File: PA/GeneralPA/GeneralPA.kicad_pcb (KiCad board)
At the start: 2 copper layers, 170.2 x 80.3 mm, 117 parts, among them J2 RFin, J3 RFout, J4 FAN, J5 SWR, J6 48v_PAD, J7 48v_PAD, Q1 2N3904, Q2 IRF510, Q3 IRF510, Q4 IRF510, Q5 2sc5706, Q6 BC548, T1 Transformer_1P_1S, T2 Transformer_1P_1S, T3 Transformer_T100, U1 LM317HVT, U2 LM7809_TO220

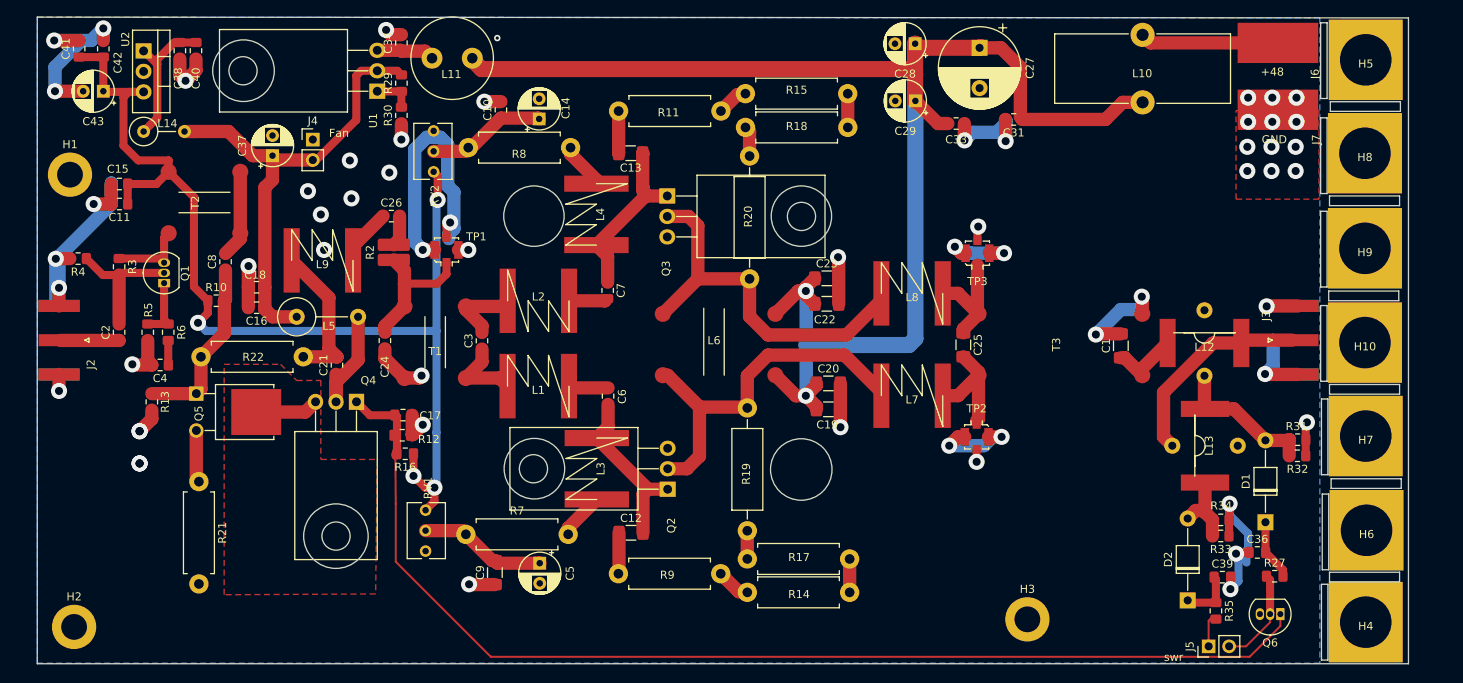
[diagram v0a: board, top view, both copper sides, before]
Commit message: update 2nd version of PA, adding some driver ciruits
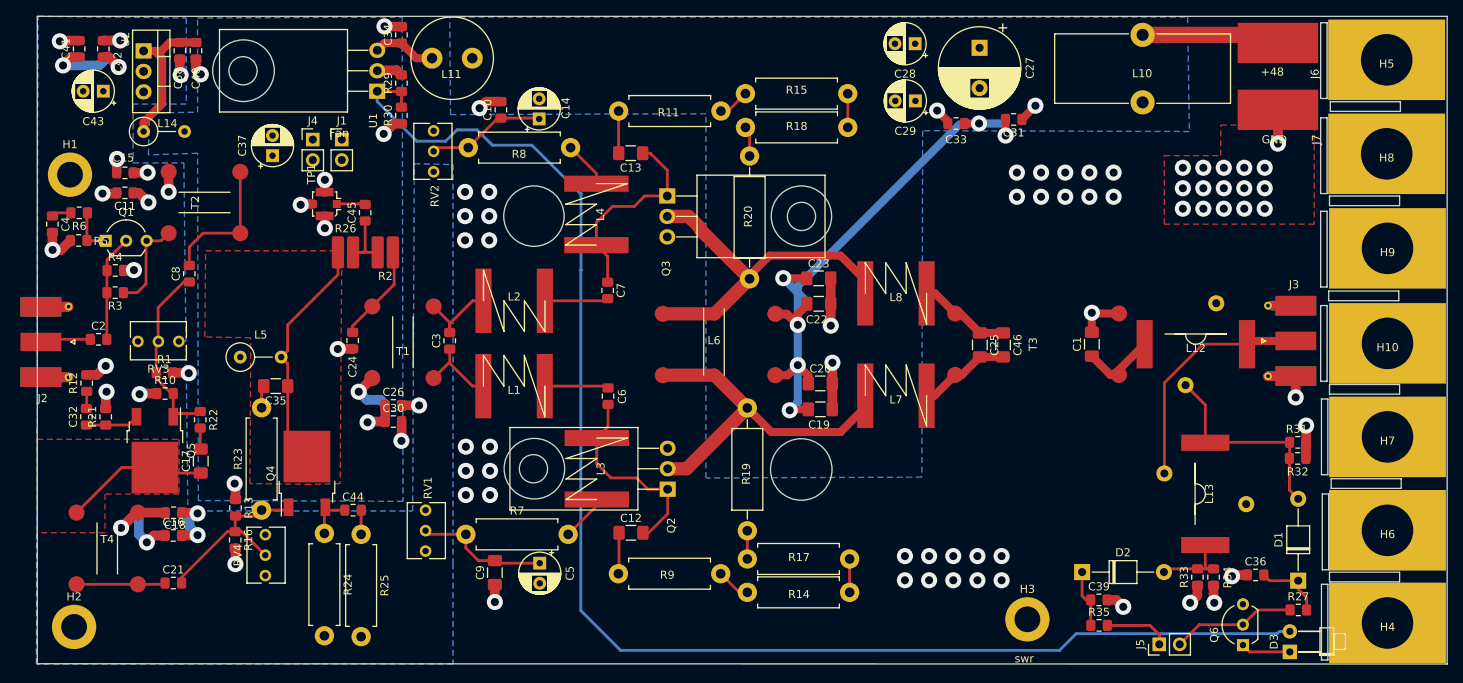
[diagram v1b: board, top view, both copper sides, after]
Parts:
- removed L9: 33n, Myfootprint:HomeMade_L_aircore
- removed TP2, TP3: Conn_Coaxial, Connector_Coaxial:U.FL_Molex_MCRF_73412-0110_Vertical
- added C30: 10n, Capacitor_SMD:C_0805_2012Metric_Pad1.15x1.40mm_HandSolder, F.Cu at (95.0, 101.0)
- added C32: 100n, Capacitor_SMD:C_0805_2012Metric_Pad1.15x1.40mm_HandSolder, F.Cu at (56.9, 100.4)
- added C35: 10u, Capacitor_SMD:C_1206_3216Metric_Pad1.42x1.75mm_HandSolder, F.Cu at (80.4, 96.6)
- added C44: 100n, Capacitor_SMD:C_0805_2012Metric_Pad1.15x1.40mm_HandSolder, F.Cu at (90.0, 112.0)
- added C45: 0.1u, Capacitor_SMD:C_0805_2012Metric_Pad1.15x1.40mm_HandSolder, F.Cu at (91.5, 75.1)
- added C46: 150p, Capacitor_SMD:C_1206_3216Metric_Pad1.42x1.75mm_HandSolder, F.Cu at (170.7, 91.5)
- added D3: LED, LED_THT:LED_D1.8mm_W1.8mm_H2.4mm_Horizontal_O3.81mm_Z1.6mm, F.Cu at (206.3, 129.6)
- added J1: FAN, Connector_PinHeader_2.54mm:PinHeader_1x02_P2.54mm_Vertical, F.Cu at (88.6, 66.0)
- added R1: 390, Resistor_SMD:R_0805_2012Metric_Pad1.15x1.40mm_HandSolder, F.Cu at (66.6, 94.9)
- added R23: 270/0.25W, Resistor_THT:R_Axial_DIN0411_L9.9mm_D3.6mm_P12.70mm_Horizontal, F.Cu at (78.6, 112.0)
- added R24: 22/1W, Resistor_THT:R_Axial_DIN0411_L9.9mm_D3.6mm_P12.70mm_Horizontal, F.Cu at (86.4, 114.9)
- added R25: 3.3/0.5W, Resistor_THT:R_Axial_DIN0411_L9.9mm_D3.6mm_P12.70mm_Horizontal, F.Cu at (91.0, 115.0)
- added R26: 0, Resistor_SMD:R_0815_2038Metric_Pad1.53x4.00mm_HandSolder, F.Cu at (89.1, 80.0)
- added RV3: 1k, Potentiometer_THT:Potentiometer_Bourns_3266Y_Vertical, F.Cu at (63.3, 91.1)
- added RV4: 1k, Potentiometer_THT:Potentiometer_Bourns_3266Y_Vertical, F.Cu at (79.1, 115.0)
- added T4: Transformer_1P_1S, GeneralPA:HomeMade_Transformer_T50, F.Cu at (59.5, 116.1)
- C17: value 0.1u -> 10u; footprint Capacitor_SMD:C_0805_2012Metric_Pad1.15x1.40mm_HandSolder -> Capacitor_SMD:C_1206_3216Metric_Pad1.42x1.75mm_HandSolder
- C2, C26, C8: value 0.1u -> 100n
- H10, H4, H5, H6, H7, H8, H9: footprint Myfootprint:T50_Laminent -> GeneralPA:T50_Laminent
- J2, J3: footprint Connector_Coaxial:SMA_Amphenol_132289_EdgeMount -> Connector_Coaxial:SMA_Molex_73251-1153_EdgeMount_Horizontal
- L1, L2, L3, L4, L7, L8: footprint Myfootprint:HomeMade_L_aircore -> GeneralPA:HomeMade_L_aircore
- L12, L13: footprint Myfootprint:HomeMade_T50_1t33t -> GeneralPA:HomeMade_T50_1t33t
- L5: footprint Inductor_THT:L_Axial_L14.0mm_D4.5mm_P7.62mm_Vertical_Fastron_LACC -> Inductor_THT:L_Axial_L7.0mm_D3.3mm_P5.08mm_Vertical_Fastron_MICC
- L6: footprint Myfootprint:HomeMade_BalChoke -> GeneralPA:HomeMade_BalChoke
- Q1, Q6: footprint Package_TO_SOT_THT:TO-92_Inline -> Package_TO_SOT_THT:TO-92_Inline_Wide
- Q4: value IRF510 -> 2sc5706; footprint Package_TO_SOT_THT:TO-220-3_Horizontal_TabDown -> Package_TO_SOT_SMD:TO-252-2
- Q5: footprint Package_TO_SOT_THT:TO-251-2-1EP_Horizontal_TabDown -> Package_TO_SOT_SMD:TO-252-2
- R12: value 680 -> 3.3
- R13: value 620 -> 1k
- R16: value 330 -> 470
- R21: value 7.1/1W -> 51; footprint Resistor_THT:R_Axial_DIN0411_L9.9mm_D3.6mm_P12.70mm_Horizontal -> Resistor_SMD:R_0805_2012Metric_Pad1.15x1.40mm_HandSolder
- R22: value 560/1W -> 270; footprint Resistor_THT:R_Axial_DIN0411_L9.9mm_D3.6mm_P12.70mm_Horizontal -> Resistor_SMD:R_0805_2012Metric_Pad1.15x1.40mm_HandSolder
- R4: value 200 -> 100
- R5: value 120 -> 100
- R6: value 5.1 -> 3.3
- T1, T2: footprint Myfootprint:HomeMade_Transformer_T50 -> GeneralPA:HomeMade_Transformer_T50
- T3: footprint Myfootprint:HomeMade_Transformer_T100 -> GeneralPA:HomeMade_Transformer_T100
- U2: value LM7809_TO220 -> LM7812_TO220
- moved R12 39.7 mm to (56.9, 96.2), turned to 90 degrees
- moved C21 33.8 mm to (67.7, 121.0), turned to 0 degrees
- moved C16 30.1 mm to (67.7, 115.1), turned to 0 degrees
- moved C18 29.8 mm to (67.7, 112.3), turned to 0 degrees
- moved C17 25.7 mm to (71.1, 105.9), turned to 90 degrees
- moved R16 23.7 mm to (75.4, 115.7), turned to 270 degrees
- moved C26 23.5 mm to (95.0, 99.0)
- moved C4 22.0 mm to (52.7, 76.5), turned to 270 degrees
- moved R6 18.5 mm to (56.0, 75.1), turned to 180 degrees
- moved R13 16.7 mm to (75.4, 111.7)
- moved TP1 16.2 mm to (86.5, 74.0), turned to 90 degrees
- moved C39 15.6 mm to (182.6, 123.1)
- moved R35 14.6 mm to (182.6, 126.3), turned to 0 degrees
- moved R5 14.3 mm to (55.9, 78.5), turned to 180 degrees
- moved R21 14.1 mm to (59.3, 100.4), turned to 90 degrees
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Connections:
- C11 pad 1: +9V -> +12V
- C15 pad 1: +9V -> +12V
- C16 pad 1: +28V -> +12V
- C17 pad 1: vshut -> Net-(C17-Pad1)
- C17 pad 2: GND -> Net-(C17-Pad2)
- C18 pad 1: +28V -> +12V
- C26 pad 1: Net-(C26-Pad1) -> +24V
- C26 pad 2: Net-(C26-Pad2) -> GND
- C37 pad 1: +28V -> +24V
- C41 pad 1: +9V -> +12V
- C42 pad 1: +9V -> +12V
- C43 pad 1: +9V -> +12V
- J4 pad 2: +28V -> +24V
- L14 pad 2: +28V -> +24V
- L5 pad 1: +28V -> +24V
- L5 pad 2: Net-(C21-Pad1) -> Net-(C35-Pad1)
- Q4 pad 1: vshut -> Net-(C21-Pad2)
- Q4 pad 2: Net-(C21-Pad1) -> Net-(C35-Pad1)
- Q4 pad 3: Net-(Q4-Pad3) -> Net-(C44-Pad1)
- Q5 pad 2: Net-(Q5-Pad2) -> Net-(C17-Pad1)
- Q5 pad 3: Net-(Q4-Pad3) -> Net-(C32-Pad1)
- Q6 pad 1: vshut -> Net-(D3-Pad1)
- R10 pad 1: +9V -> +12V
- R12 pad 1: vshut -> Net-(C32-Pad2)
- R13 pad 1: Net-(C8-Pad1) -> +24V
- R13 pad 2: GND -> Net-(C21-Pad2)
- R16 pad 1: +9V -> Net-(C21-Pad2)
- R16 pad 2: vshut -> GND
- R2 pad 2: Net-(C26-Pad2) -> Net-(C45-Pad1)
- R21 pad 1: Net-(Q5-Pad2) -> Net-(C32-Pad1)
- R22 pad 2: Net-(C21-Pad2) -> Net-(C17-Pad2)
- R29 pad 1: Net-(R29-Pad1) -> vshut
- R29 pad 2: +28V -> +24V
- R30 pad 2: Net-(R29-Pad1) -> vshut
- RV1 pad 1: +9V -> +12V
- RV2 pad 1: +9V -> +12V
- T1 pad 2: GND -> +24V
- T2 pad 2: +9V -> +12V
- TP1 pad 1: Net-(C24-Pad1) -> Net-(C45-Pad2)
- U1 pad 1: Net-(R29-Pad1) -> vshut
- U1 pad 2: +28V -> +24V
- U2 pad 3: +9V -> +12V
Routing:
- net +9V: track 137.1 -> 0.00 mm, vias 4 -> 0
- net +48V: track 179.3 -> 73.3 mm, vias 2 -> 6
- net GND: track 226.7 -> 127.2 mm, vias 60 -> 83
- net +28V: track 60.2 -> 0.00 mm
- net vshut: track 146.9 -> 180.3 mm
- net +12V: track 0.00 -> 32.9 mm, vias 0 -> 8
- net Net-(C35-Pad1): track 0.00 -> 29.6 mm
- net Net-(C17-Pad1): track 0.00 -> 18.0 mm
- net +24V: track 0.00 -> 15.9 mm, vias 0 -> 3
- net Net-(C26-Pad1): track 10.0 -> 0.00 mm
- net Net-(Q4-Pad3): track 7.89 -> 0.00 mm
- net Net-(D1-Pad2): track 18.3 -> 26.1 mm
- net Net-(C45-Pad1): track 0.00 -> 7.05 mm
- net Net-(C32-Pad1): track 0.00 -> 6.64 mm
- net Net-(Q5-Pad2): track 6.48 -> 0.00 mm
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- added copper zone on B.Cu, net +12V
- added copper zone on B.Cu, net +24V
- added copper zone on B.Cu, net +48V
- added copper zone on GND.Cu, net GND
- added copper zone on GND2.Cu, net GND
- added copper zone on F.Cu, net Net-(C17-Pad1)
- added copper zone on F.Cu, net Net-(C35-Pad1)
- removed copper zone on B.Cu, net GND
- removed copper zone on F.Cu, net Net-(Q4-Pad3)
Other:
- board size 170.2 x 80.3 mm -> 175 x 80.4 mm
- copper layers 2 -> 4
- net class Default: trace_width 0.25 -> 0.35
- net class Signal removed

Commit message: add missed files
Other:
- board size 175 x 80.4 mm -> 177.6 x 80.4 mm
